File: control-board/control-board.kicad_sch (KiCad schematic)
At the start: 14 parts, among them U2 LM7805_TO220, U3 LD1117V33, U4 74HC595, U5 D168K

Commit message: Major updates (like 4 hrs work), added motors and lots of protections
Signed-off-by: Ravinder Olivier Singh Dadiala <ravinder-Olivier@outlook.com>
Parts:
- removed D2: 1N5239, symbol Device:D_Zener
- added C10, C9: 0.01uF, symbol Device:C
- added C11: 47uF, symbol Device:C_Polarized
- added C12, C13, C7: 0.1uF, symbol Device:C
- added C8: 1000uF, symbol Device:C_Polarized
- added D2: ICTE-12, symbol Device:D_TVS
- added D3, D4, D5, D6: 1N5819, Diode_THT:D_DO-41_SOD81_P10.16mm_Horizontal, symbol Diode:1N5819
- added D7, D8: D_TVS, symbol Device:D_TVS
- added J1, J2: Conn_01x06, symbol Connector_Generic:Conn_01x06
- added NT1: NetTie_2, symbol Device:NetTie_2
- added R1, R2: 100R, symbol Device:R
- added U1: ROB-14450, ROB-14450:MODULE_ROB-14450, symbol ROB-14450:ROB-14450
- A1: footprint Module:RaspberryPi_Pico_Common_Unspecified -> Module:RaspberryPi_Pico_SMD_HandSolder
- D1: value 1N4007 -> 1N5822
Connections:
- net GND: now also C5.2, C6.2, C11.2, C7.2, C8.2, D2.2 (A2), J1.3 (Pin_3), J2.3 (Pin_3), NT1.1, U1.3 (GND), U1.8 (GND__1), U1.9 (GND__2); no longer A1.33 (AGND)
- net at C3.1, C4.1, C5.1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: now also U4.10 (~{SRCLR}), U4.16 (VCC), C10.1, C7.1, J1.5 (Pin_5), J2.4 (Pin_4), U1.2 (VCC); no longer C6.1
- net at C2.1, U2.3 (VO), U3.3 (VI): now also A1.39 (VSYS), C6.1, C11.1
- net at A1.17 (GPIO13): now also U1.13 (STBY)
- net at A1.19 (GPIO14): now also U1.11 (BI2)
- net at A1.20 (GPIO15): now also U1.12 (BI1)
- net at A1.25 (GPIO19): now also U1.16 (PWMA)
- net at A1.26 (GPIO20): now also U1.10 (PWMB)
- net at A1.27 (GPIO21): now also U1.14 (AI1)
- net at A1.29 (GPIO22): now also U1.15 (AI2)
- net at A1.31 (GPIO26_ADC0): now also C12.1, R1.1
- net at A1.32 (GPIO27_ADC1): now also C13.1, R2.1
- net at C1.2, D1.1 (K), U2.1 (VI): now also C8.1, D2.1 (A1), D3.1 (K), D4.1 (K), D5.1 (K), D6.1 (K), U1.1 (VM)
- new net: C9.1, D8.2 (A2), J2.5 (Pin_5), R2.2
- new net: D5.2 (A), J2.1 (Pin_1), U1.7 (B01)
- new net: D6.2 (A), J2.2 (Pin_2), U1.6 (B02)
- new net: D3.2 (A), J1.1 (Pin_1), U1.4 (A01)
- new net: D7.2 (A2), J1.4 (Pin_4), R1.2
- new net: D4.2 (A), J1.2 (Pin_2), U1.5 (A02)
- new net GNDS: A1.33 (AGND), C10.2, C12.2, C13.2, C9.2, D7.1 (A1), D8.1 (A1), J1.6 (Pin_6), J2.6 (Pin_6), NT1.2
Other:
- note added: "FADER BOARD CONNECTOR HEADERS VERSION 1"
- note added: "MOTOR CONTROL MODULE VERSION 1"
- note added: "POWER REGULATION 9V -> 3.3V VERSION 5: MAX 800MA"
- note removed: "POWER REGULATION 9V -> 3.3V VERSION 2: MAX 800MA"
- moved on the sheet: A1, C5, C6

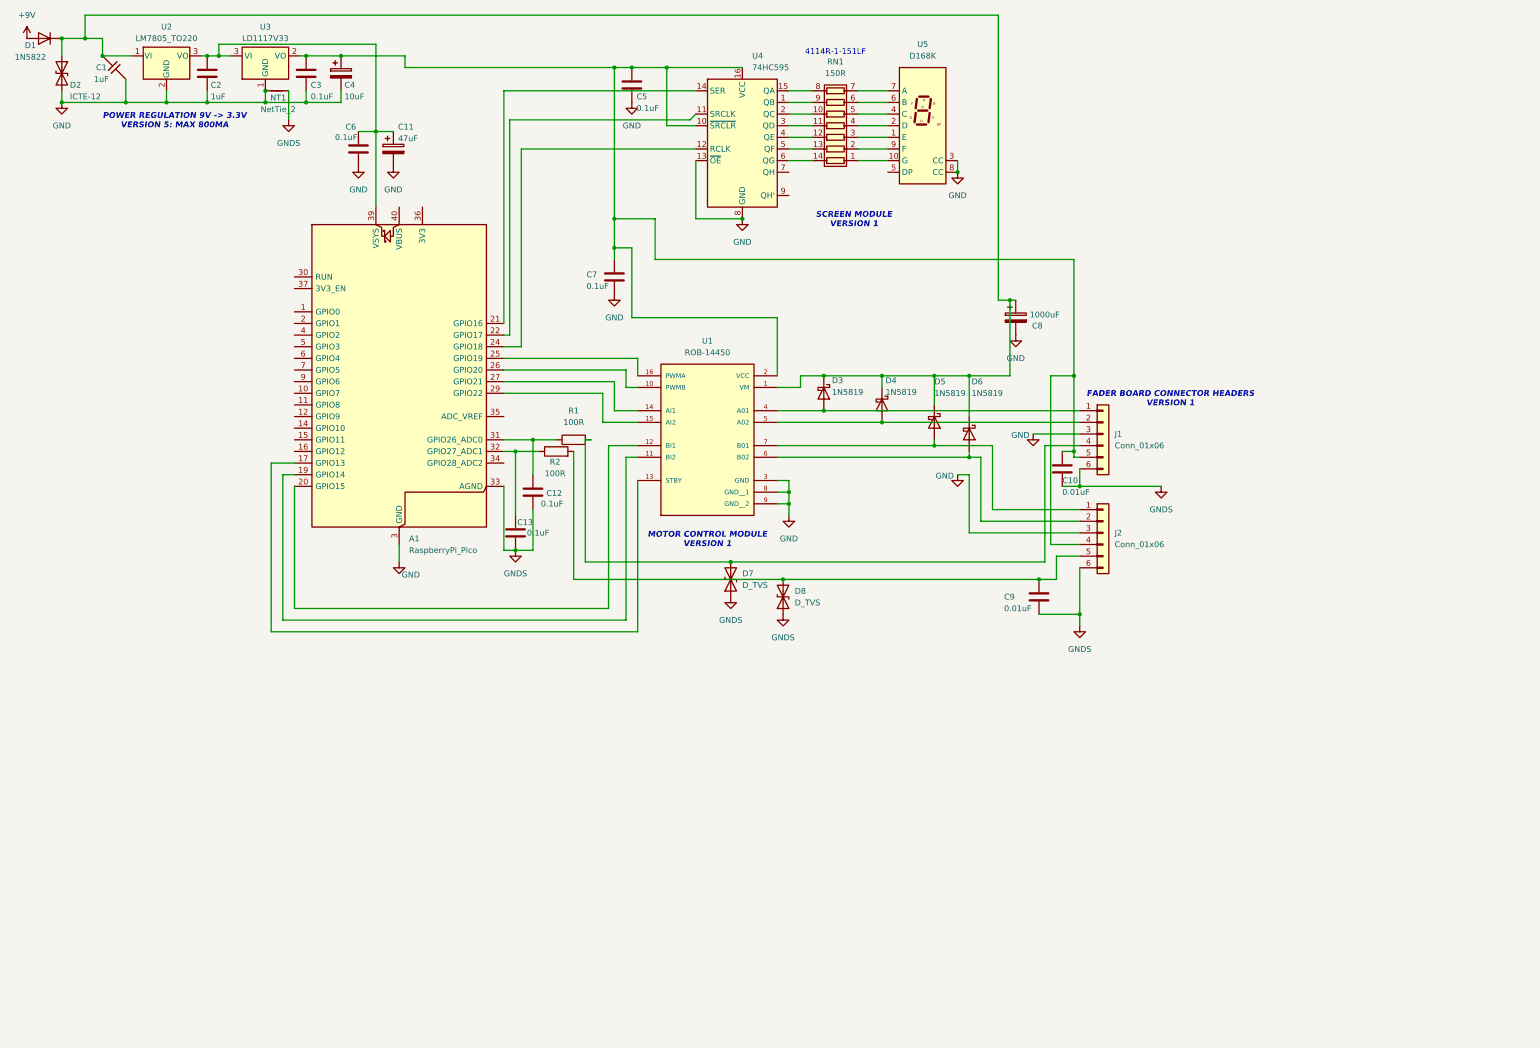
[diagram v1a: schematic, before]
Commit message: Added Voltage Sag (transistor switched resistor network to linear regulator), into a voltage inverter to provide -9v for the PNP tonebender
Signed-off-by: Ravinder Olivier Singh Dadiala <ravinder-Olivier@outlook.com>
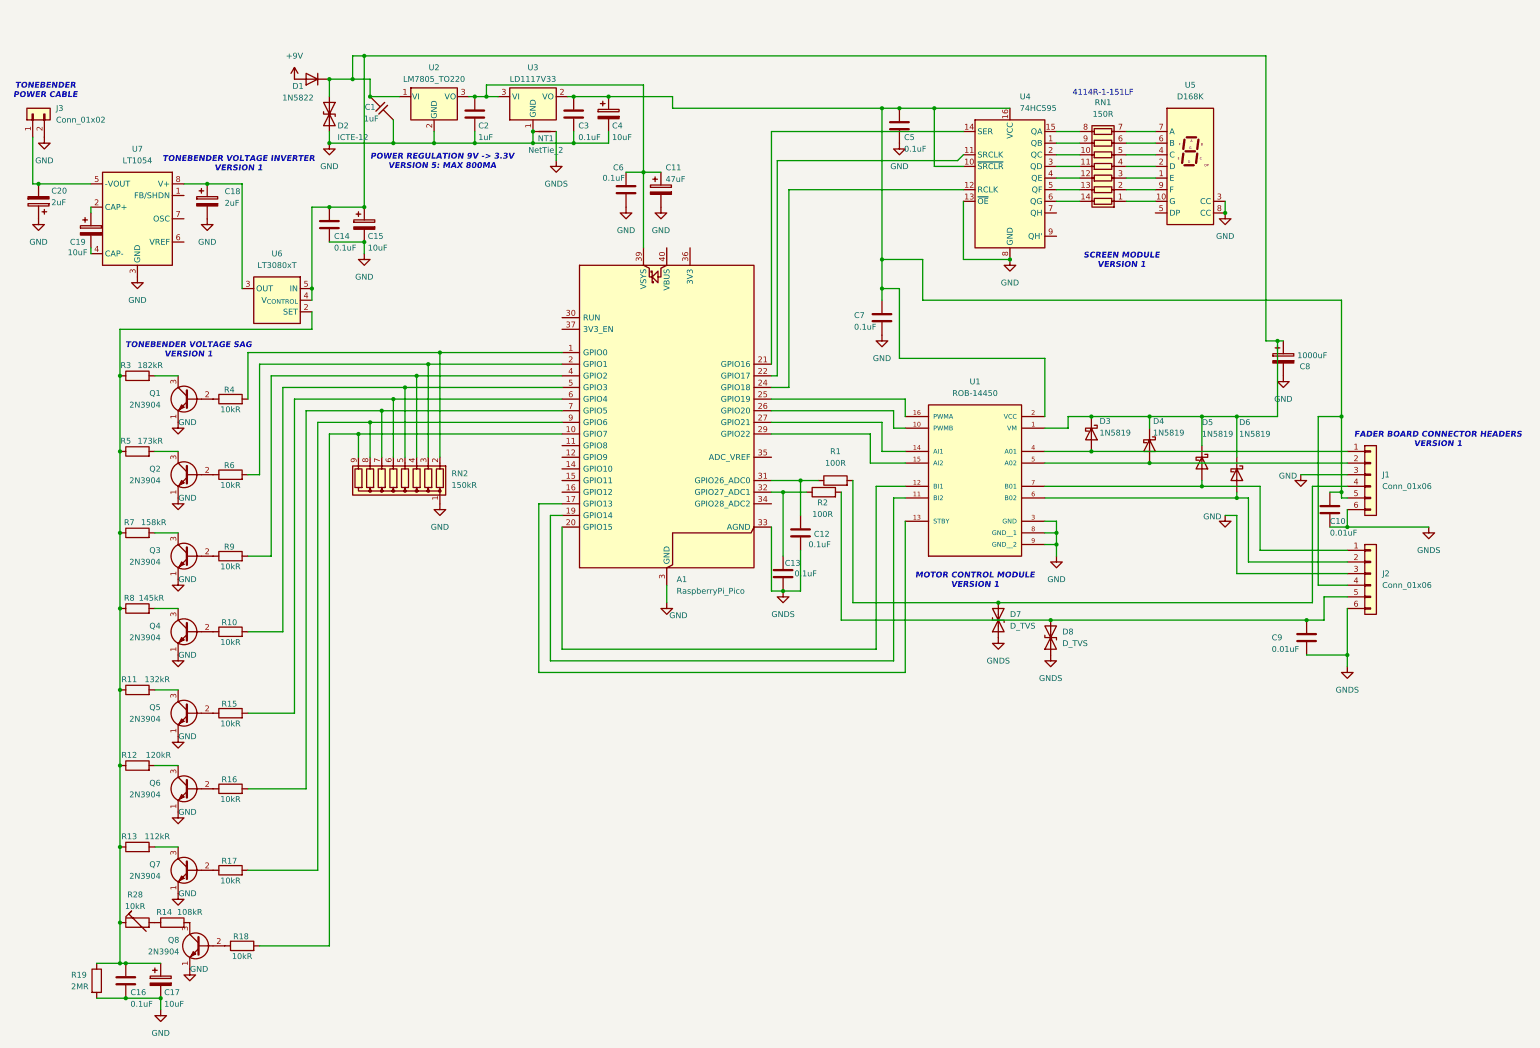
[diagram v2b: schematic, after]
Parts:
- added C14, C16: 0.1uF, symbol Device:C
- added C15, C17, C19: 10uF, symbol Device:C_Polarized
- added C18, C20: 2uF, symbol Device:C_Polarized
- added J3: Conn_01x02, symbol Connector_Generic:Conn_01x02
- added Q1, Q2, Q3, Q4, Q5, Q6, Q7, Q8: 2N3904, Package_TO_SOT_THT:TO-92_Inline, symbol Transistor_BJT:2N3904
- added R10, R15, R16, R17, R18, R4, R6, R9: 10kR, symbol Device:R
- added R11: 132kR, symbol Device:R
- added R12: 120kR, symbol Device:R
- added R13: 112kR, symbol Device:R
- added R14: 108kR, symbol Device:R
- added R19: 2MR, symbol Device:R
- added R28: 10kR, symbol Device:R_Trim
- added R3: 182kR, symbol Device:R
- added R5: 173kR, symbol Device:R
- added R7: 158kR, symbol Device:R
- added R8: 145kR, symbol Device:R
- added RN2: 150kR, Resistor_THT:R_Array_SIP9, symbol Device:R_Network08
- added U6: LT3080xT, Package_TO_SOT_THT:TO-220-5_P3.4x3.7mm_StaggerOdd_Lead3.8mm_Vertical, symbol Regulator_Linear:LT3080xT
- added U7: LT1054, symbol Regulator_SwitchedCapacitor:LT1054
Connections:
- net GND: now also C14.2, C15.2, C16.2, C17.2, C18.2, C20.1, J3.2 (Pin_2), Q1.1 (E), Q2.1 (E), Q3.1 (E), Q4.1 (E), Q5.1 (E), Q6.1 (E), Q7.1 (E), Q8.1 (E), R19.2, RN2.1 (common), U7.3 (GND)
- net at C1.2, C8.1, D1.1 (K)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: now also C14.1, C15.1, U6.4 (V_{CONTROL}), U6.5 (IN)
- net at A1.1 (GPIO0): now also R4.2, RN2.2 (R1)
- net at A1.10 (GPIO7): now also R18.2, RN2.9 (R8)
- net at A1.2 (GPIO1): now also R6.2, RN2.3 (R2)
- net at A1.4 (GPIO2): now also R9.2, RN2.4 (R3)
- net at A1.5 (GPIO3): now also R10.2, RN2.5 (R4)
- net at A1.6 (GPIO4): now also R15.2, RN2.6 (R5)
- net at A1.7 (GPIO5): now also R16.2, RN2.7 (R6)
- net at A1.9 (GPIO6): now also R17.2, RN2.8 (R7)
- new net: C16.1, C17.1, R11.1, R12.1, R13.1, R19.1, R28.1, R3.1, R5.1, R7.1, R8.1, U6.2 (SET)
- new net: Q5.3 (C), R11.2
- new net: Q4.2 (B), R10.1
- new net: Q7.2 (B), R17.1
- new net: C20.2, J3.1 (Pin_1), U7.5 (-VOUT)
- new net: Q4.3 (C), R8.2
- new net: Q6.2 (B), R16.1
- new net: Q6.3 (C), R12.2
- new net: C19.1, U7.2 (CAP+)
- new net: C19.2, U7.4 (CAP-)
- new net: C18.1, U6.3 (OUT), U6.6 (OUT), U7.8 (V+)
- new net: Q1.2 (B), R4.1
- new net: Q1.3 (C), R3.2
- new net: R14.1, R28.2
- new net: Q2.2 (B), R6.1
- new net: Q2.3 (C), R5.2
- new net: Q8.3 (C), R14.2
- new net: Q8.2 (B), R18.1
- new net: Q5.2 (B), R15.1
- new net: Q7.3 (C), R13.2
- new net: Q3.2 (B), R9.1
- new net: Q3.3 (C), R7.2
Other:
- note added: "TONEBENDER POWER CABLE"
- note added: "TONEBENDER VOLTAGE INVERTER VERSION 1"
- note added: "TONEBENDER VOLTAGE SAG VERSION 1"
- moved on the sheet: A1, C1, C10, C11, C12, C13, C2, C3, C4, C5, C6, C7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

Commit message: major schem updates
changed tonebender power supply (now it's voltage inverter --> voltage
sag), however this needed me to change my transistor resistor switch
network into a optotransistor controlled version.

added a controller ic to free up a lot of gpio pins and control the
entire resistor switching network with only 2 pins (!)

Signed-off-by: Ravinder Olivier Singh Dadiala <ravinder-Olivier@outlook.com>
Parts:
- removed Q1, Q2, Q3, Q4, Q5, Q6, Q7, Q8: 2N3904, Package_TO_SOT_THT:TO-92_Inline, symbol Transistor_BJT:2N3904
- removed R13: 112kR, symbol Device:R
- removed R14: 108kR, symbol Device:R
- removed R15, R16, R17, R18: 10kR, symbol Device:R
- removed R28: 10kR, symbol Device:R_Trim
- removed RN2: 150kR, Resistor_THT:R_Array_SIP9, symbol Device:R_Network08
- removed U6: LT3080xT, Package_TO_SOT_THT:TO-220-5_P3.4x3.7mm_StaggerOdd_Lead3.8mm_Vertical, symbol Regulator_Linear:LT3080xT
- added RN2: 220R, symbol Device:R_Pack08
- added U10: PCF8574AP, Package_DIP:DIP-16_W7.62mm, symbol Interface_Expansion:PCF8574AP
- added U6: LT3091xT7, Package_TO_SOT_THT:TO-220-7_P2.54x3.7mm_StaggerOdd_Lead3.8mm_Vertical, symbol Regulator_Linear:LT3091xT7
- added U8, U9: LTV-847M, Package_DIP:DIP-16_W10.16mm, symbol Isolator:LTV-847M
- R10: value 10kR -> 82.5kR
- R11: value 132kR -> 4.7kR
- R12: value 120kR -> 4.7kR
- R3: value 182kR -> 196kR
- R4: value 10kR -> 178kR
- R5: value 173kR -> 162kR
- R6: value 10kR -> 147kR
- R7: value 158kR -> 127kR
- R8: value 145kR -> 110kR
- R9: value 10kR -> 97.6kR
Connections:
- net GND: now also U10.1 (A0), U10.2 (A1), U10.3 (A2), U10.8 (GND), U6.6 (GND), U8.10, U8.12, U8.14, U8.16, U8.2, U8.4, U8.6, U8.8, U9.10, U9.12, U9.14, U9.16, U9.2, U9.4, U9.6, U9.8
- net at C16.1, C17.1, R19.1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: now also R10.1, R4.1, R6.1, R9.1, U6.5 (SET); no longer R11.1, R12.1
- net at R11.2: now also A1.1 (GPIO0), U10.14 (SCL)
- net at R10.2: now also U9.9; no longer A1.5 (GPIO3)
- net at C1.2, C8.1, D1.1 (K)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: now also C18.1, U7.8 (V+); no longer C14.1, C15.1
- net at R4.2: now also U8.13; no longer A1.1 (GPIO0)
- net at A1.2 (GPIO1): now also R12.2, U10.15 (SDA); no longer R6.2
- net at A1.36 (3V3): now also R11.1, R12.1, U10.16 (VDD)
- net at A1.4 (GPIO2): no longer R9.2
- net at C20.2, U7.5 (-VOUT): now also U6.4 (IN); no longer J3.1 (Pin_1)
- net at R8.2: now also U9.13
- net at R3.2: now also U8.15
- net at R5.2: now also U8.11
- net at R7.2: now also U9.15
- new net: RN2.14 (R3.2), U9.3
- new net: RN2.9 (R8.2), U8.1
- new net: C14.1, C15.1, J3.1 (Pin_1), U6.7 (OUT)
- new net: R6.2, U8.9
- new net: RN2.13 (R4.2), U9.1
- new net: RN2.11 (R6.2), U8.5
- new net: R9.2, U9.11
- new net: RN2.15 (R2.2), U9.5
- new net: RN2.12 (R5.2), U8.7
- new net: RN2.3 (R3.1), U10.10 (P5)
- new net: RN2.2 (R2.1), U10.11 (P6)
- new net: RN2.1 (R1.1), U10.12 (P7)
- new net: RN2.8 (R8.1), U10.4 (P0)
- new net: RN2.7 (R7.1), U10.5 (P1)
- new net: RN2.6 (R6.1), U10.6 (P2)
- new net: RN2.5 (R5.1), U10.7 (P3)
- new net: RN2.4 (R4.1), U10.9 (P4)
- new net: RN2.10 (R7.2), U8.3
- new net: RN2.16 (R1.2), U9.7
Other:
- note added: "TONEBENDER VOLTAGE INVERTER VERSION 2"
- note added: "TONEBENDER VOLTAGE SAG VERSION 3"
- note removed: "TONEBENDER VOLTAGE INVERTER VERSION 1"
- note removed: "TONEBENDER VOLTAGE SAG VERSION 1"
- moved on the sheet: A1, C1, C10, C11, C12, C13, C14, C15, C16, C17, C18, C19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
